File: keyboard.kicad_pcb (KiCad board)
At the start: 2 copper layers, 285 x 94.6 mm, 256 parts, among them IC1 ATMEGA32U4, J1 USB_2, P1 DIL16, P2 DIL16, P3 CONN_6, SW1 SW_PUSH, X1 ASX4

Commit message: support 5/6 split or 6/7 split
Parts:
- removed the HOLE at (185.0, 82.2)
- added HOLE: VAL**, hole:PKRH, F.Cu at (178.1, 81.3)
- added HOLE: VAL**, hole:PKRH, F.Cu at (184.1, 86.1)
- added HOLE: VAL**, hole:PKRH, F.Cu at (189.7, 82.2)
- added HOLE: VAL**, hole:PKRH, F.Cu at (174.6, 64.6)
- added HOLE: VAL**, hole:PKRH, F.Cu at (177.9, 64.6)
- added HOLE: VAL**, hole:PKRH, F.Cu at (175.9, 80.3)
- added HOLE: VAL**, hole:PKRH, F.Cu at (175.9, 67.3)
- moved DW5 15.0 mm to (159.4, 84.1)
- moved R1 15.0 mm to (155.4, 84.1)
- moved HOLE 0.32 mm to (193.3, 81.3)
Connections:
- D32 pad 1: /col7-r -> /col7
- D33 pad 1: /col7-r -> /col7
- P2 pad 16: /col7-r -> /col7
- P2 pad 7: /row1-r -> /row1
- S36 pad 1: /row1-r -> /row1
- S41 pad 1: /row1-r -> /row1
- S46 pad 1: /row1-r -> /row1
- S51 pad 1: /row1-r -> /row1
- S56 pad 1: /row1-r -> /row1
- S61 pad 1: /row1-r -> /row1
- S66 pad 1: /row1-r -> /row1
- S661 pad 1: /row1-r -> /row1
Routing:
- net /row1: track 249.0 -> 494.4 mm, vias 6 -> 9
- net /row1-r: track 231.1 -> 0.00 mm, vias 3 -> 0
- net /col7: track 222.0 -> 380.7 mm, vias 6 -> 10
- net /col7-r: track 92.4 -> 0.00 mm, vias 4 -> 0
- net GND: track 1144.3 -> 1116.3 mm, vias 55 -> 58
- net /GPIO0: track 307.7 -> 292.3 mm
- net VCC: track 402.5 -> 389.1 mm
- net Net-(D27-Pad2): track 13.1 -> 14.2 mm, vias 0 -> 1
- net /row2: track 215.2 -> 214.2 mm

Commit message: add r4_leftshift and related r5 layout
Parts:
- removed the HOLE at (200.0, 123.4)
- removed the HOLE at (196.7, 123.4)
- removed S6512: MX1A, mx1a:MX1A_no3d
- added D351: 1N4148, 0805:0805D, B.Cu at (204.8, 153.1)
- added D45: 1N4148, 0805:0805D, B.Cu at (254.9, 153.0)
- added HOLE: VAL**, hole:PKRH, F.Cu at (197.6, 125.2)
- added HOLE: VAL**, hole:PKRH, F.Cu at (200.0, 155.2)
- added HOLE: VAL**, hole:PKRH, F.Cu at (200.0, 138.3)
- added HOLE: VAL**, hole:PKRH, F.Cu at (174.8, 84.1)
- added HOLE: VAL**, hole:PKRH, F.Cu at (197.5, 142.4)
- added HOLE: VAL**, hole:PKRH, F.Cu at (193.6, 159.2)
- added HOLE: VAL**, hole:PKRH, F.Cu at (196.9, 159.2)
- added HOLE: VAL**, hole:PKRH, F.Cu at (193.5, 123.5)
- added MXST: VAL**, mx1a:MXST, F.Cu at (209.6, 150.0)
- added MXST: VAL**, mx1a:MXST, F.Cu at (233.4, 150.0)
- added MXST: VAL**, mx1a:MXST, F.Cu at (157.2, 150.0)
- added MXST: VAL**, mx1a:MXST, F.Cu at (181.0, 150.0)
- added MXST: VAL**, mx1a:MXST, F.Cu at (69.1, 131.0)
- added MXST: VAL**, mx1a:MXST, F.Cu at (92.9, 131.0)
- added S141: MX1A, mx1a:MX1A_no3d, F.Cu at (109.5, 131.0)
- added S191: MX1A, mx1a:MX1A_no3d, F.Cu at (128.6, 131.0)
- added S241: MX1A, mx1a:MX1A_no3d, F.Cu at (147.6, 131.0)
- added S291: MX1A, mx1a:MX1A_no3d, F.Cu at (166.7, 131.0)
- added S303: MX1A, mx1a:MX1A_no3d, F.Cu at (169.1, 150.0)
- added S341: MX1A, mx1a:MX1A_no3d, F.Cu at (185.7, 131.0)
- added S353: MX1A, mx1a:MX1A_no3d, F.Cu at (209.6, 150.0)
- added S391: MX1A, mx1a:MX1A_no3d, F.Cu at (204.8, 131.0)
- added S403: MX1A, mx1a:MX1A_no3d, F.Cu at (221.5, 150.0)
- added S412: MX1A, mx1a:MX1A_no3d, F.Cu at (81.0, 131.0)
- added S441: MX1A, mx1a:MX1A_no3d, F.Cu at (223.8, 131.0)
- added S45: MX1A, mx1a:MX1A, F.Cu at (250.0, 150.0)
- added S451: MX1A, mx1a:MX1A_no3d, F.Cu at (259.6, 150.0)
- added S491: MX1A, mx1a:MX1A_no3d, F.Cu at (242.9, 131.0)
- added S512: MX1A, mx1a:MX1A_no3d, F.Cu at (78.6, 150.0)
- added S541: MX1A, mx1a:MX1A_no3d, F.Cu at (261.9, 131.0)
- added S551: MX1A, mx1a:MX1A_no3d, F.Cu at (264.3, 150.0)
- added S591: MX1A, mx1a:MX1A_no3d, F.Cu at (281.0, 131.0)
- added S602: MX1A, mx1a:MX1A_no3d, F.Cu at (300.0, 150.0)
- added S642: MX1A, mx1a:MX1A_no3d, F.Cu at (300.0, 131.0)
- added S651: MX1A, mx1a:MX1A_no3d, F.Cu at (311.9, 150.0)
- added S652: MX1A, mx1a:MX1A_no3d, F.Cu at (319.1, 150.0)
- added S693: MX1A, mx1a:MX1A_no3d, F.Cu at (319.1, 131.0)
- moved P1 38.1 mm to (120.2, 137.7)
- moved S302 28.6 mm to (181.0, 150.0)
- moved S301 26.2 mm to (154.8, 150.0)
- moved S55 23.8 mm to (273.8, 150.0)
- moved S60 23.8 mm to (297.7, 150.0)
- moved S65 23.8 mm to (321.5, 150.0)
- moved S401 16.7 mm to (226.2, 150.0)
- moved S552 16.7 mm to (281.0, 150.0)
- moved S70 16.7 mm to (338.1, 150.0)
- moved D65 15.0 mm to (307.0, 153.0)
- moved D55 12.5 mm to (269.5, 153.0)
- moved S402 9.53 mm to (235.7, 150.0)
- moved D5 9.00 mm to (69.6, 153.0)
- moved D30 7.00 mm to (150.0, 153.0)
- moved D9 4.57 mm to (86.4, 123.0), turned to 0 degrees
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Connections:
- J1 pad 5: (no net) -> GND
- S64 pad 1: Net-(D64-Pad2) -> /row4-r
- S64 pad 2: /row4-r -> Net-(D64-Pad2)
- S641 pad 1: /row4-r -> Net-(D64-Pad2)
- S641 pad 2: Net-(D64-Pad2) -> /row4-r
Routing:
- net GND: track 1116.3 -> 1069.6 mm, vias 58 -> 68
- net /col9-r: track 110.7 -> 149.9 mm
- net /row5-r: track 260.0 -> 289.0 mm
- net /row4-r: track 145.7 -> 174.4 mm
- net VCC: track 389.1 -> 362.4 mm, vias 12 -> 11
- net /col7: track 380.7 -> 403.3 mm, vias 10 -> 12
- net Net-(D45-Pad2): track 0.00 -> 21.1 mm
- net /col11: track 101.3 -> 82.7 mm
- net /GPIO0: track 292.3 -> 275.5 mm
- net /col3: track 145.8 -> 161.8 mm
- net /col13-r: track 179.8 -> 195.7 mm
- net /row2: track 214.2 -> 198.6 mm
- net /col13: track 98.2 -> 83.4 mm
- net /col10: track 102.0 -> 89.0 mm
- net /col12: track 99.0 -> 86.7 mm
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
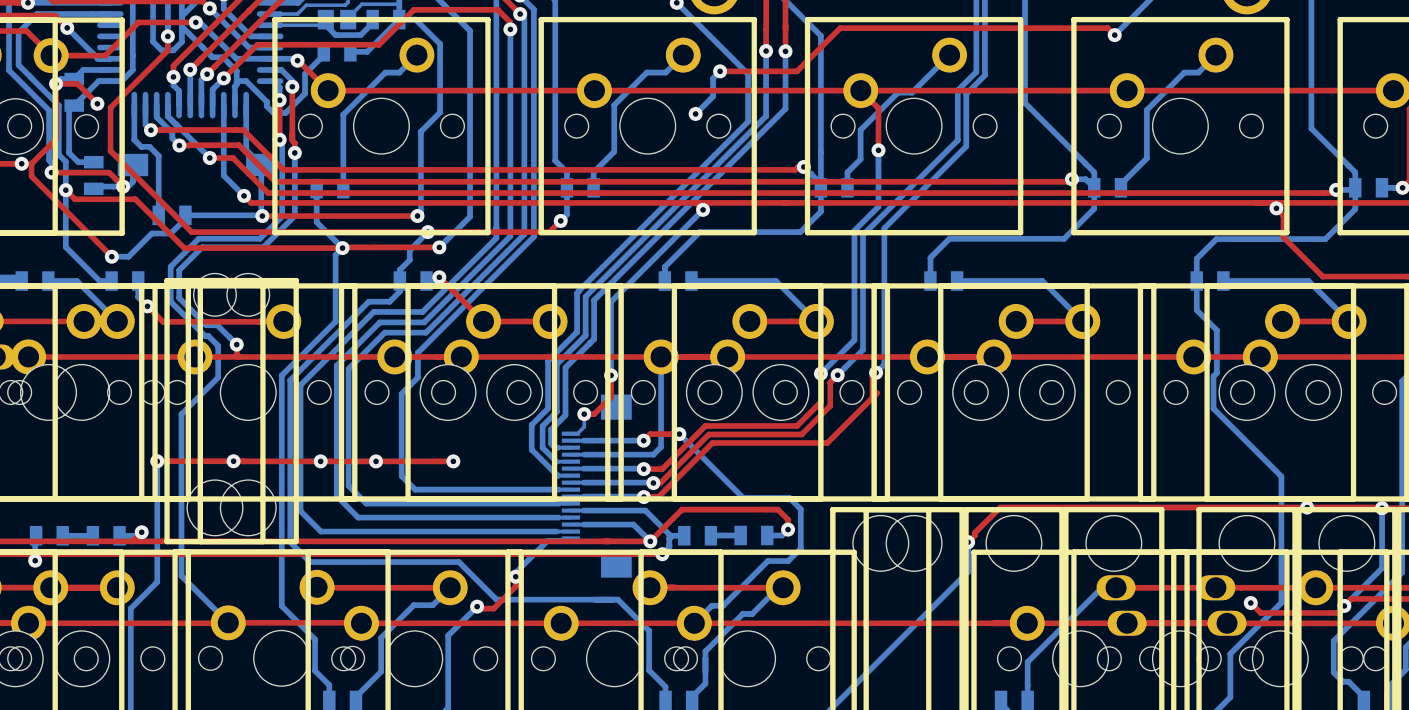
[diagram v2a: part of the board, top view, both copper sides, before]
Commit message: change to 4x4mm 4-pin button
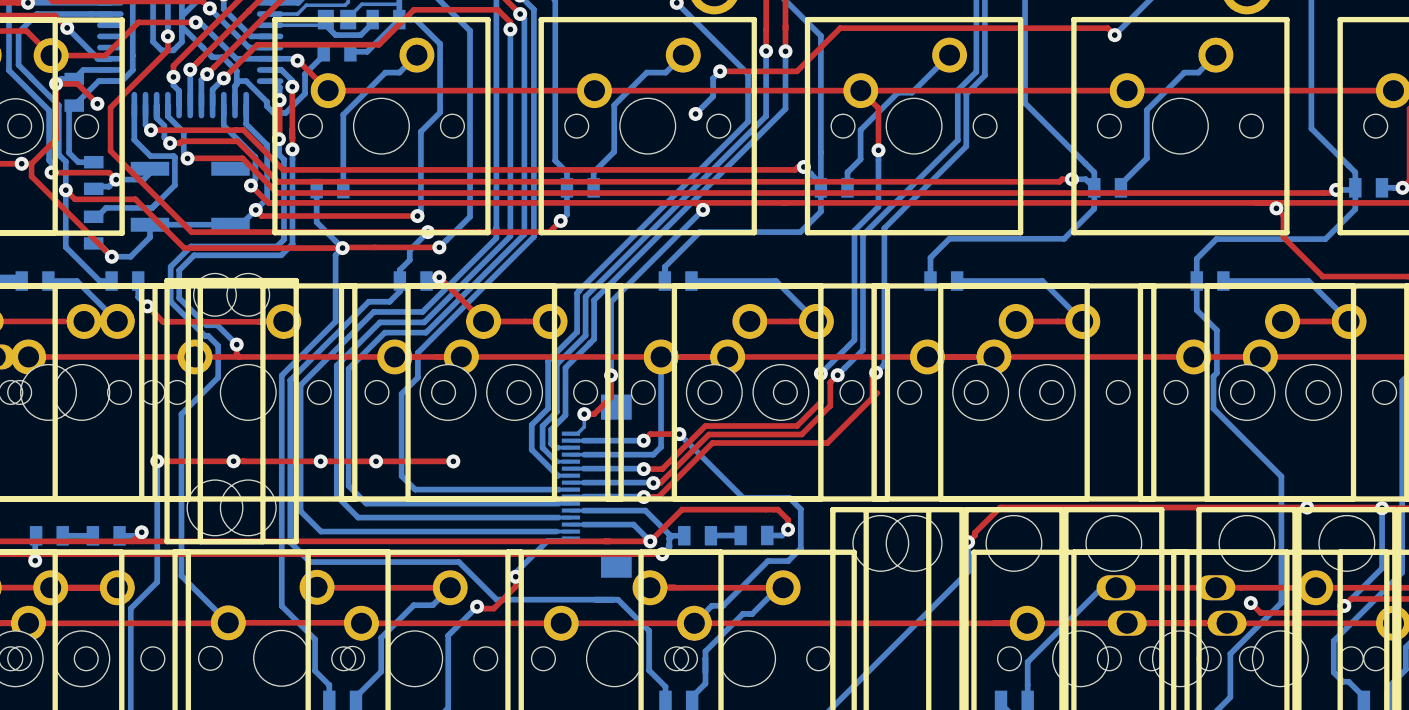
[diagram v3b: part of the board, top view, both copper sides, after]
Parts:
- SW1: footprint Buttons_Switches_SMD:SW_SPST_FSMSM -> Buttons_Switches_SMD:SW_SPST_EVPBF
- moved R13 5.71 mm to (84.2, 119.4), turned to 90 degrees
- moved SW1 2.32 mm to (91.1, 117.0)
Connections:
- SW1 pad 1: GND -> Net-(IC1-Pad13)
- SW1 pad 2: Net-(IC1-Pad13) -> GND
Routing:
- net Net-(IC1-Pad33): track 8.96 -> 15.4 mm
- net GND: track 1069.6 -> 1072.1 mm
- net /col5: track 131.1 -> 133.3 mm
- net /row4: track 179.5 -> 180.8 mm
- net /row5: track 214.6 -> 215.8 mm

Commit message: change usb to type-c
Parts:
- J1: footprint usb:67503 -> usb:USB_C_Receptacle_Palconn_UTC16-G
- moved D1 7.86 mm to (65.8, 78.4)
- moved J1 3.18 mm to (80.6, 67.9), turned to 0 degrees
- moved D6 1.24 mm to (96.5, 78.4)
- turned MXST to 270 degrees (x2)
- turned S1 to 0 degrees
- turned S6 to 0 degrees
- turned S67 to 0 degrees
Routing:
- net GND: track 1072.1 -> 1138.1 mm, vias 68 -> 71
- net /row2-r: track 234.6 -> 224.2 mm
- net Net-(D67-Pad2): track 4.30 -> 14.0 mm
- net /row1: track 488.6 -> 498.0 mm, vias 8 -> 7
- net Net-(D1-Pad2): track 7.05 -> 13.4 mm
- net /col10-r: track 196.6 -> 192.4 mm
- net /col1: track 111.9 -> 115.7 mm
- net Net-(J1-Pad2): track 3.29 -> 6.61 mm
- net VCC: track 362.4 -> 359.2 mm
- net /col7: track 402.9 -> 399.7 mm
- net Net-(D15-Pad2): track 23.5 -> 20.5 mm
- net /GPIO0: track 275.5 -> 272.6 mm
- net /col9-r: track 149.9 -> 147.3 mm
- net /row4: track 180.8 -> 178.4 mm
- net Net-(J1-Pad3): track 3.62 -> 5.77 mm
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
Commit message: add mounting hole at edges
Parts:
- added REF**: MountingHole_2.5mm, Mounting_Holes:MountingHole_2.5mm, F.Cu at (325.4, 150.0)
- added REF**: MountingHole_2.5mm, Mounting_Holes:MountingHole_2.5mm, F.Cu at (165.4, 150.0)
- added REF**: MountingHole_2.5mm, Mounting_Holes:MountingHole_2.5mm, F.Cu at (155.4, 150.0)
- added REF**: MountingHole_2.5mm, Mounting_Holes:MountingHole_2.5mm, F.Cu at (115.5, 150.0)
- added REF**: MountingHole_2.5mm, Mounting_Holes:MountingHole_2.5mm, F.Cu at (105.5, 150.0)
- added REF**: MountingHole_2.5mm, Mounting_Holes:MountingHole_2.5mm, F.Cu at (85.5, 150.0)
- added REF**: MountingHole_2.5mm, Mounting_Holes:MountingHole_2.5mm, F.Cu at (95.5, 150.0)
- added REF**: MountingHole_2.5mm, Mounting_Holes:MountingHole_2.5mm, F.Cu at (309.6, 73.8)
- added REF**: MountingHole_2.5mm, Mounting_Holes:MountingHole_2.5mm, F.Cu at (214.3, 73.8)
- added REF**: MountingHole_2.5mm, Mounting_Holes:MountingHole_2.5mm, F.Cu at (195.3, 73.8)
- added REF**: MountingHole_2.5mm, Mounting_Holes:MountingHole_2.5mm, F.Cu at (176.2, 73.8)
- added REF**: MountingHole_2.5mm, Mounting_Holes:MountingHole_2.5mm, F.Cu at (315.4, 150.0)
- added REF**: MountingHole_2.5mm, Mounting_Holes:MountingHole_2.5mm, F.Cu at (157.2, 73.8)
- added REF**: MountingHole_2.5mm, Mounting_Holes:MountingHole_2.5mm, F.Cu at (81.0, 73.8)
- added REF** (x2): MountingHole_2.5mm, Mounting_Holes:MountingHole_2.5mm, F.Cu at (305.4, 150.0)
- added REF**: MountingHole_2.5mm, Mounting_Holes:MountingHole_2.5mm, F.Cu at (255.4, 150.0)
- added REF**: MountingHole_2.5mm, Mounting_Holes:MountingHole_2.5mm, F.Cu at (245.4, 150.0)
- added REF**: MountingHole_2.5mm, Mounting_Holes:MountingHole_2.5mm, F.Cu at (235.4, 150.0)
- added REF**: MountingHole_2.5mm, Mounting_Holes:MountingHole_2.5mm, F.Cu at (225.4, 150.0)
- added REF**: MountingHole_2.5mm, Mounting_Holes:MountingHole_2.5mm, F.Cu at (175.4, 150.0)
- moved D35 14.4 mm to (187.3, 144.0)
- moved D55 14.2 mm to (280.5, 144.0)
- moved D15 13.5 mm to (116.0, 144.0)
- moved D10 11.4 mm to (95.0, 144.0)
- moved D45 11.4 mm to (247.9, 144.0)
- moved D60 11.1 mm to (287.5, 144.0)
- moved D70 10.5 mm to (334.5, 144.0)
- moved D40 9.85 mm to (218.0, 144.1)
- moved D65 9.85 mm to (311.0, 144.0)
- moved D30 9.66 mm to (146.5, 144.0)
- moved D351 9.03 mm to (204.1, 144.1)
- moved D5 9.00 mm to (69.6, 144.0)
- moved R11 2.42 mm to (82.3, 77.5)
- moved R10 2.30 mm to (79.7, 77.5)
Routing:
- net GND: track 1138.1 -> 1171.4 mm, vias 71 -> 72
- net Net-(D35-Pad2): track 33.0 -> 7.65 mm
- net /col7: track 399.7 -> 379.7 mm
- net /col6: track 201.8 -> 183.3 mm
- net /col8-r: track 137.3 -> 119.9 mm
- net /col11-r: track 137.9 -> 123.2 mm
- net /col3: track 159.8 -> 145.2 mm
- net /col13-r: track 194.5 -> 180.2 mm
- net Net-(D70-Pad2): track 18.1 -> 5.66 mm
- net /col9-r: track 147.3 -> 135.4 mm
- net Net-(D40-Pad2): track 32.5 -> 22.1 mm
- net Net-(D60-Pad2): track 24.9 -> 14.5 mm
- net /col14-r: track 212.1 -> 203.4 mm
- net /col1: track 115.7 -> 107.1 mm
- net Net-(D65-Pad2): track 20.9 -> 12.4 mm
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
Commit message: add 6 5x5mm ws2812b
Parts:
- removed DW1, DW2, DW3, DW4, DW5, DW6, DW7, DW8: LED, 0805:0805D
- removed R1, R3: R, 0805:0805R
- removed R2, R4, R6, R7, R8, R9: R, 0805:0805D
- added C10: 100nF, 0805:0805C, B.Cu at (239.8, 120.7)
- added C11: 100nF, 0805:0805C, B.Cu at (129.4, 120.7)
- added C12: 100nF, 0805:0805C, B.Cu at (271.8, 120.7)
- added C13: 100nF, 0805:0805C, B.Cu at (153.4, 120.7)
- added C14: 100nF, 0805:0805C, B.Cu at (309.9, 120.7)
- added C9: 100nF, 0805:0805C, B.Cu at (95.2, 120.7)
- added LED1: WS2812B, LEDs:LED_WS2812B-PLCC4, B.Cu at (100.3, 121.3)
- added LED2: WS2812B, LEDs:LED_WS2812B-PLCC4, B.Cu at (234.7, 121.3)
- added LED3: WS2812B, LEDs:LED_WS2812B-PLCC4, B.Cu at (134.5, 121.3)
- added LED4: WS2812B, LEDs:LED_WS2812B-PLCC4, B.Cu at (266.7, 121.3)
- added LED5: WS2812B, LEDs:LED_WS2812B-PLCC4, B.Cu at (158.5, 121.3)
- added LED6: WS2812B, LEDs:LED_WS2812B-PLCC4, B.Cu at (304.8, 121.3)
- moved D39 2.03 mm to (207.5, 123.0)
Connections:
- P1 pad 14: /GPIO0 -> /GPIO0_out
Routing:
- net /GPIO0: track 272.6 -> 58.4 mm, vias 9 -> 4
- net /GPIO0-r: track 289.1 -> 79.8 mm, vias 7 -> 4
- net /VCC-r: track 287.1 -> 110.4 mm, vias 4 -> 5
- net GND: track 1171.4 -> 1345.7 mm, vias 72 -> 89
- net /GPIO0_out: track 0.00 -> 56.4 mm, vias 0 -> 2
- net Net-(LED4-Pad2): track 0.00 -> 35.4 mm, vias 0 -> 2
- net Net-(LED1-Pad2): track 0.00 -> 33.5 mm, vias 0 -> 2
- net Net-(LED2-Pad2): track 0.00 -> 31.3 mm, vias 0 -> 2
- net VCC: track 357.5 -> 386.1 mm
- net Net-(LED3-Pad2): track 0.00 -> 21.9 mm, vias 0 -> 2
- net /col8-r: track 119.9 -> 125.9 mm
- net Net-(D59-Pad2): track 15.2 -> 10.5 mm
- net Net-(D29-Pad2): track 14.9 -> 10.2 mm
- net Net-(D24-Pad2): track 14.9 -> 10.2 mm
- net Net-(D44-Pad2): track 15.1 -> 10.4 mm
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
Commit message: change C9-C15's field value from 100nF to 100n
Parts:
- C10, C11, C12, C13, C14, C9: value 100nF -> 100n
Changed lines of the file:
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@@
   )
   (layers
-    (0 F.Cu signal)
-    (31 B.Cu signal)
+    (0 F.Cu signal hide)
+    (31 B.Cu signal hide)
     (32 B.Adhes user hide)
     (33 F.Adhes user hide)
@@
     (39 F.Mask user)
     (40 Dwgs.User user hide)
-    (41 Cmts.User user)
+    (41 Cmts.User user hide)
     (42 Eco1.User user hide)
     (43 Eco2.User user hide)
@@
       (effects (font (size 0.8 0.8) (thickness 0.15)) (justify mirror))
     )
-    (fp_text value 100nF (at 0 0 270) (layer B.SilkS) hide
+    (fp_text value 100n (at 0 0 270) (layer B.SilkS) hide
       (effects (font (size 0.635 0.635) (thickness 0.127)) (justify mirror))
     )
@@
       (effects (font (size 0.8 0.8) (thickness 0.15)) (justify mirror))
     )
-    (fp_text value 100nF (at 0 0 450) (layer B.SilkS) hide
+    (fp_text value 100n (at 0 0 450) (layer B.SilkS) hide
       (effects (font (size 0.635 0.635) (thickness 0.127)) (justify mirror))
     )
@@
       (effects (font (size 0.8 0.8) (thickness 0.15)) (justify mirror))
     )
-    (fp_text value 100nF (at 0 0 270) (layer B.SilkS) hide
+    (fp_text value 100n (at 0 0 270) (layer B.SilkS) hide
       (effects (font (size 0.635 0.635) (thickness 0.127)) (justify mirror))
     )
@@
       (effects (font (size 0.8 0.8) (thickness 0.15)) (justify mirror))
     )
-    (fp_text value 100nF (at 0 0 450) (layer B.SilkS) hide
+    (fp_text value 100n (at 0 0 450) (layer B.SilkS) hide
       (effects (font (size 0.635 0.635) (thickness 0.127)) (justify mirror))
     )
@@
       (effects (font (size 0.8 0.8) (thickness 0.15)) (justify mirror))
     )
-    (fp_text value 100nF (at 0 0 270) (layer B.SilkS) hide
+    (fp_text value 100n (at 0 0 270) (layer B.SilkS) hide
       (effects (font (size 0.635 0.635) (thickness 0.127)) (justify mirror))
     )
@@
       (effects (font (size 0.8 0.8) (thickness 0.15)) (justify mirror))
     )
-    (fp_text value 100nF (at 0 0 450) (layer B.SilkS) hide
+    (fp_text value 100n (at 0 0 450) (layer B.SilkS) hide
       (effects (font (size 0.635 0.635) (thickness 0.127)) (justify mirror))
     )
